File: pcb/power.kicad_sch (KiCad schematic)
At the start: 30 parts, among them Q5 AO3407A, SW3 POWER, U1 TPS2121RUXR, U2 TPS2121RUXR, U3 TPS2121RUXR, U4 74LVC1G08

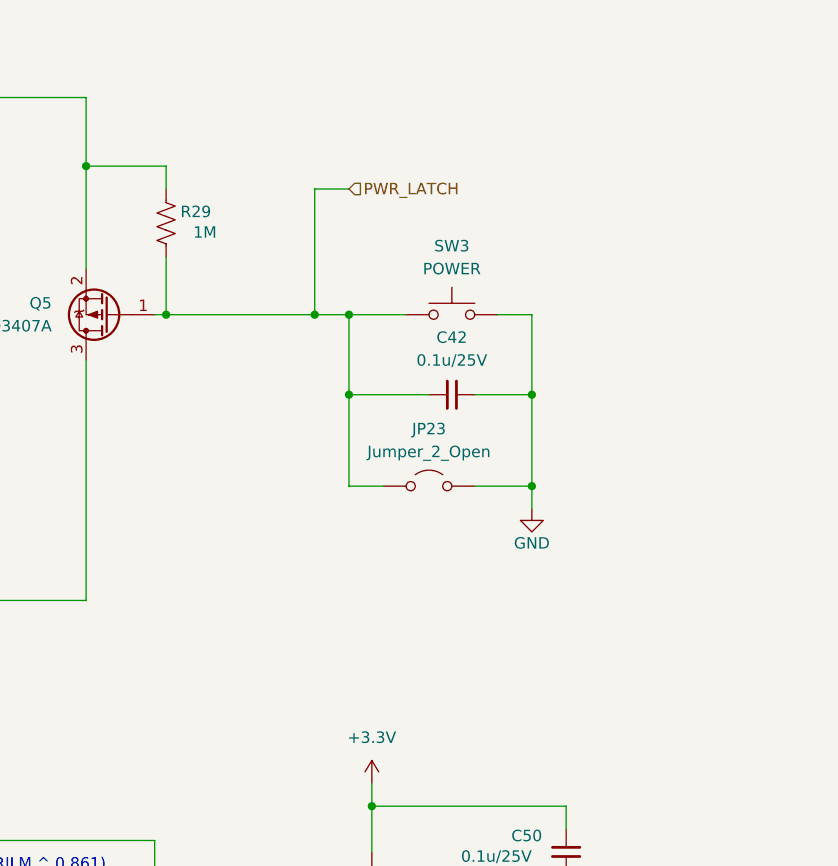
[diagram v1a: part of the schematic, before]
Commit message: Fix second mass-symbol-update reversion (recurred at same scale)
Same class of damage as the previous fix (commit 4ab9510) -- another
project-wide symbol resync reverted ~65 Datasheet fields and 5 Footprints
(Y2 crystal back to the wrong 5.0x3.2mm package again, U9/U12/U10/Y1
footprints back to non-stock equivalents) across all 7 schematic files.
Restored every field to its previously-verified value.

Also caught two real, independent bugs surfaced while re-checking (not
caused by this reversion, pre-existing): R32/R33/R43/R18 (10k YAGEO
RT0603BRD0710KL pull-ups, C95204) all had a mismatched Datasheet pointing
to a different resistor's PDF (RC0805FR-0710KL, wrong package family);
C36's Datasheet had drifted back to a different capacitor's PDF again
(same bug fixed once already this session).

ERC clean, same 14 pre-existing errors, no regressions.

Co-Authored-By: Claude Sonnet 5 <noreply@anthropic.com>
Claude-Session: https://claude.ai/code/session_01LhLkuH6sQ5GbUZ61bG7p2h
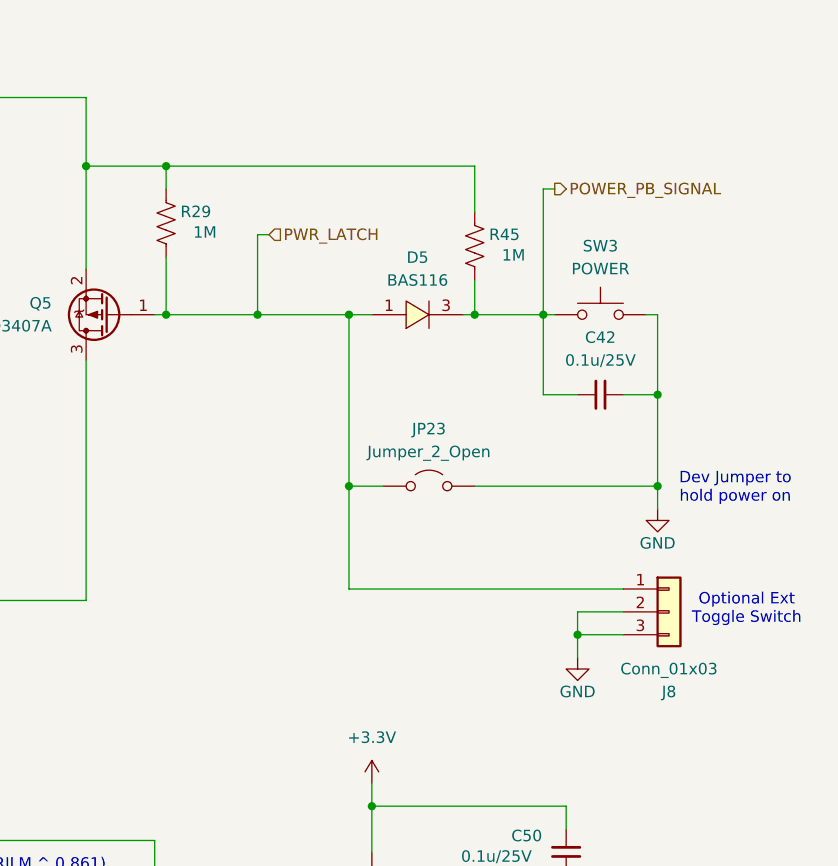
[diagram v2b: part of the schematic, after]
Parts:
- added D5: BAS116, kicad_gx_library:SOT-23_L2.9-W1.3-P1.90-LS2.4-BR, symbol kicad_gx_library:BAS116LT1G
- added J8: Conn_01x03, Connector_JST:JST_PH_B3B-PH-SM4-TB_1x03-1MP_P2.00mm_Vertical, symbol Connector_Generic:Conn_01x03
- added R45: 1M, Resistor_SMD:R_0603_1608Metric, symbol Device:R_US
- R29: LCSC Part # C98220 -> C105578; MPN RC0603FR-0710KL -> RC0603FR-071ML
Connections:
- net GND: now also J8.2 (Pin_2), J8.3 (Pin_3)
- net PWR_LATCH: now also D5.1, J8.1 (Pin_1); no longer C42.1, SW3.2
- net at Q5.2 (S), R29.2, U3.1 (OUT)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: now also R45.2
- new net POWER_PB_SIGNAL: C42.1, D5.3, R45.1, SW3.2
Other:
- note added: "Dev Jumper to hold power on"
- note added: "Optional Ext Toggle Switch"
- moved on the sheet: C42, SW3
